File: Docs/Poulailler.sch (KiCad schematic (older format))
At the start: 13 parts, among them Q1 Q_PNP_ECB

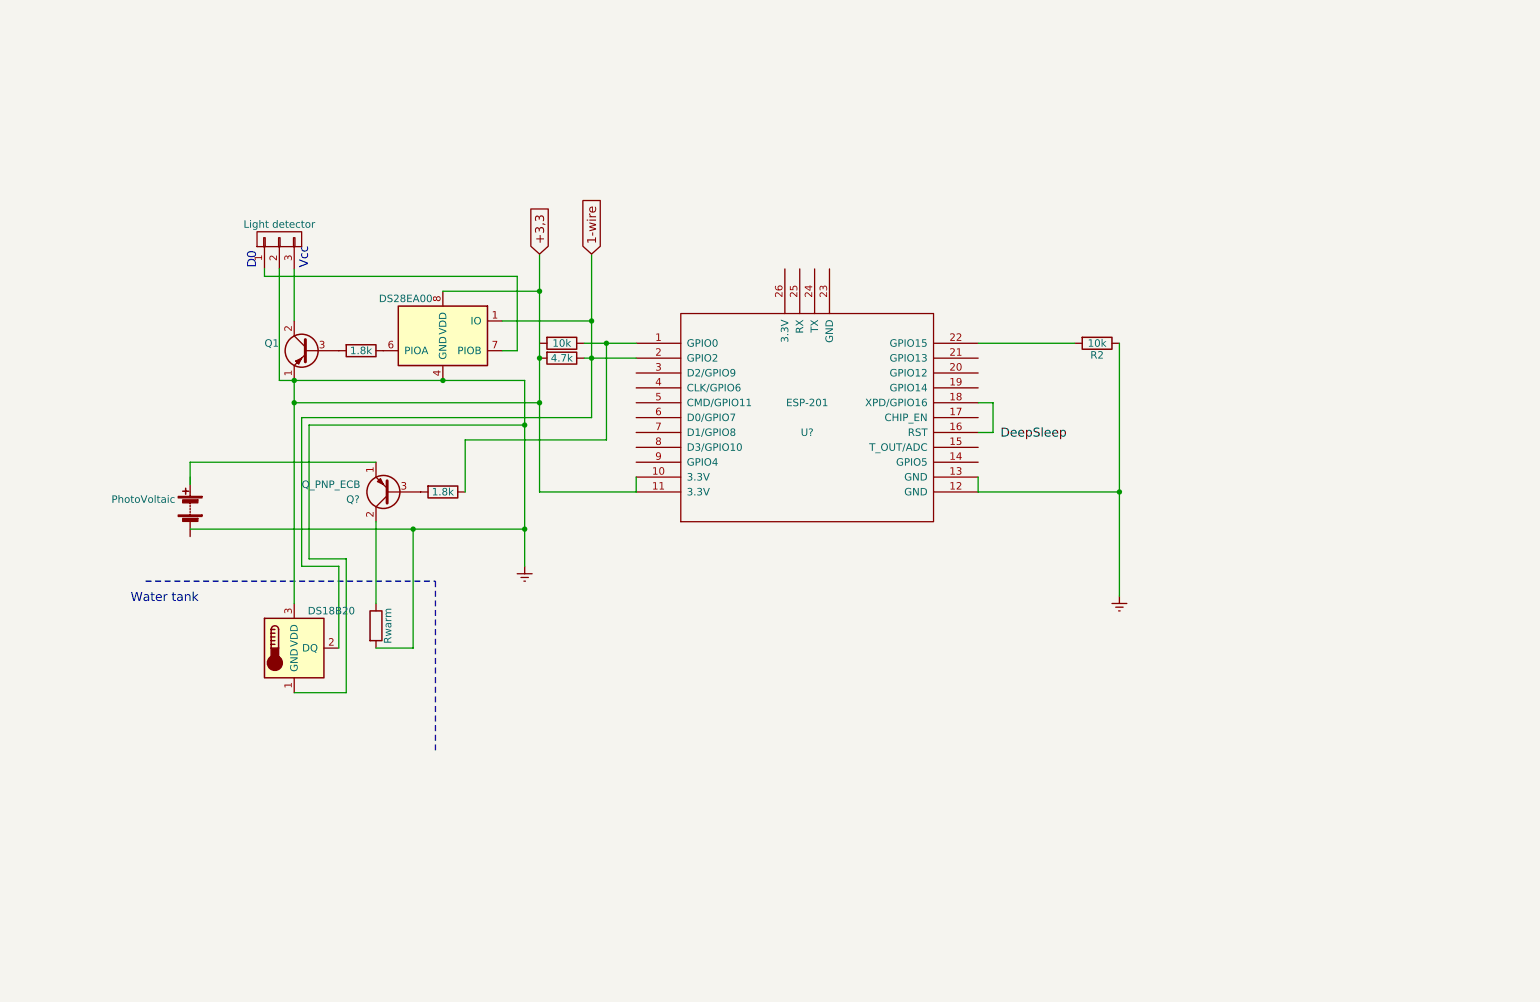
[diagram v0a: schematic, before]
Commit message: Split by function
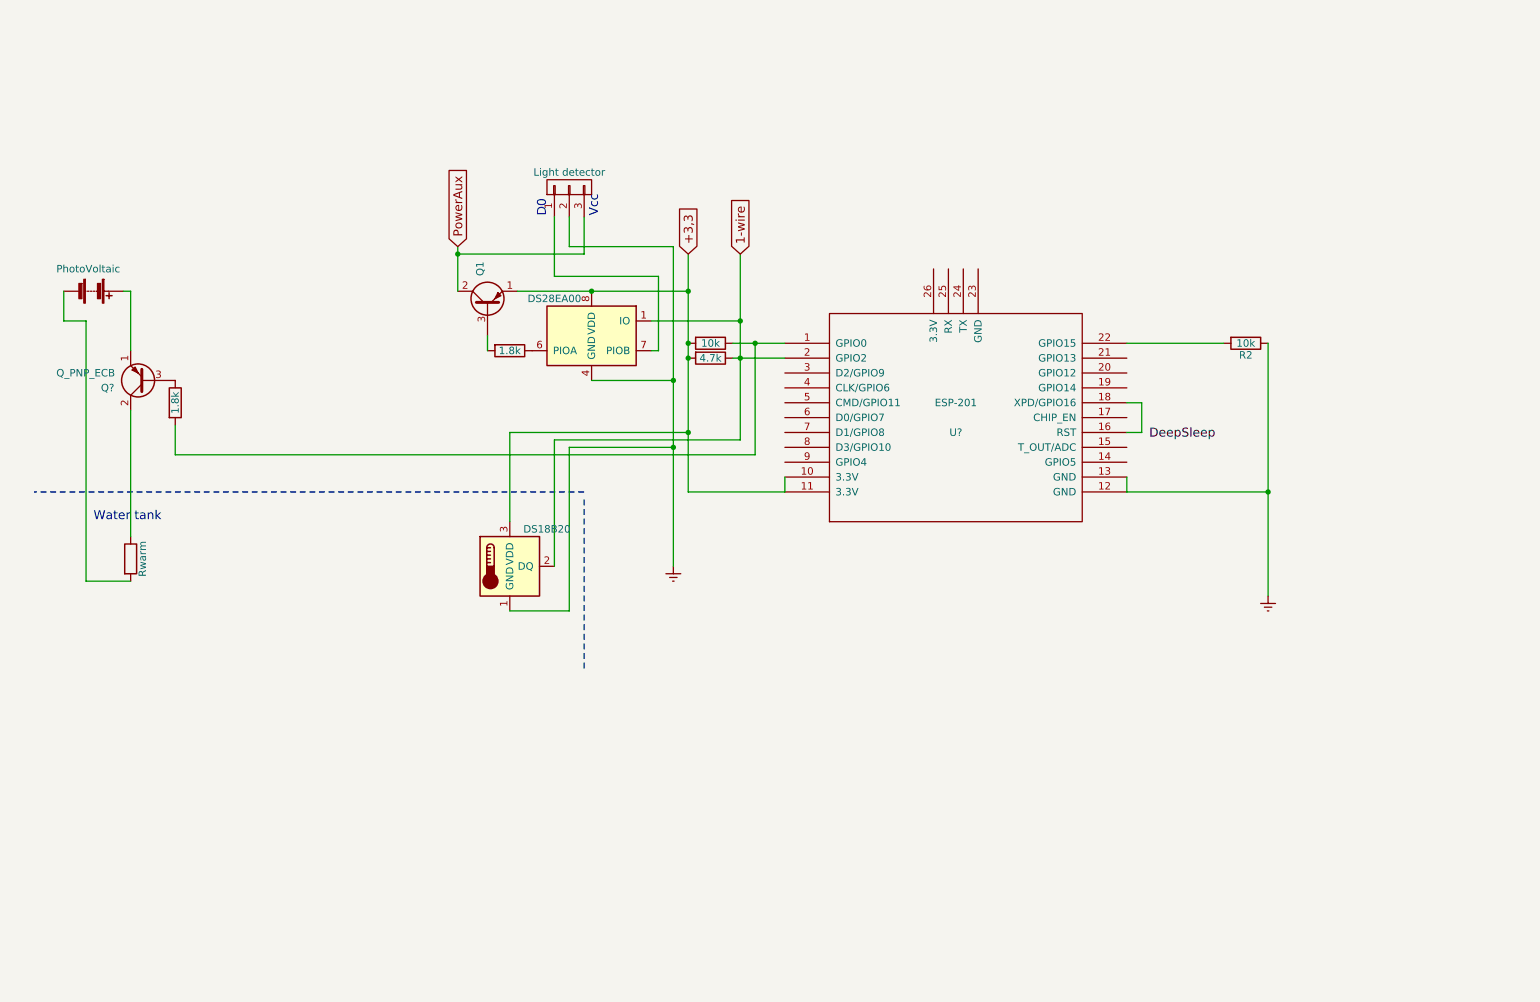
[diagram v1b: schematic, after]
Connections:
- net labels added: PowerAux
- wire segments 43 -> 44
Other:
- moved on the sheet: PhotoVoltaic, Q1, Q?, R2, Rwarm, U?

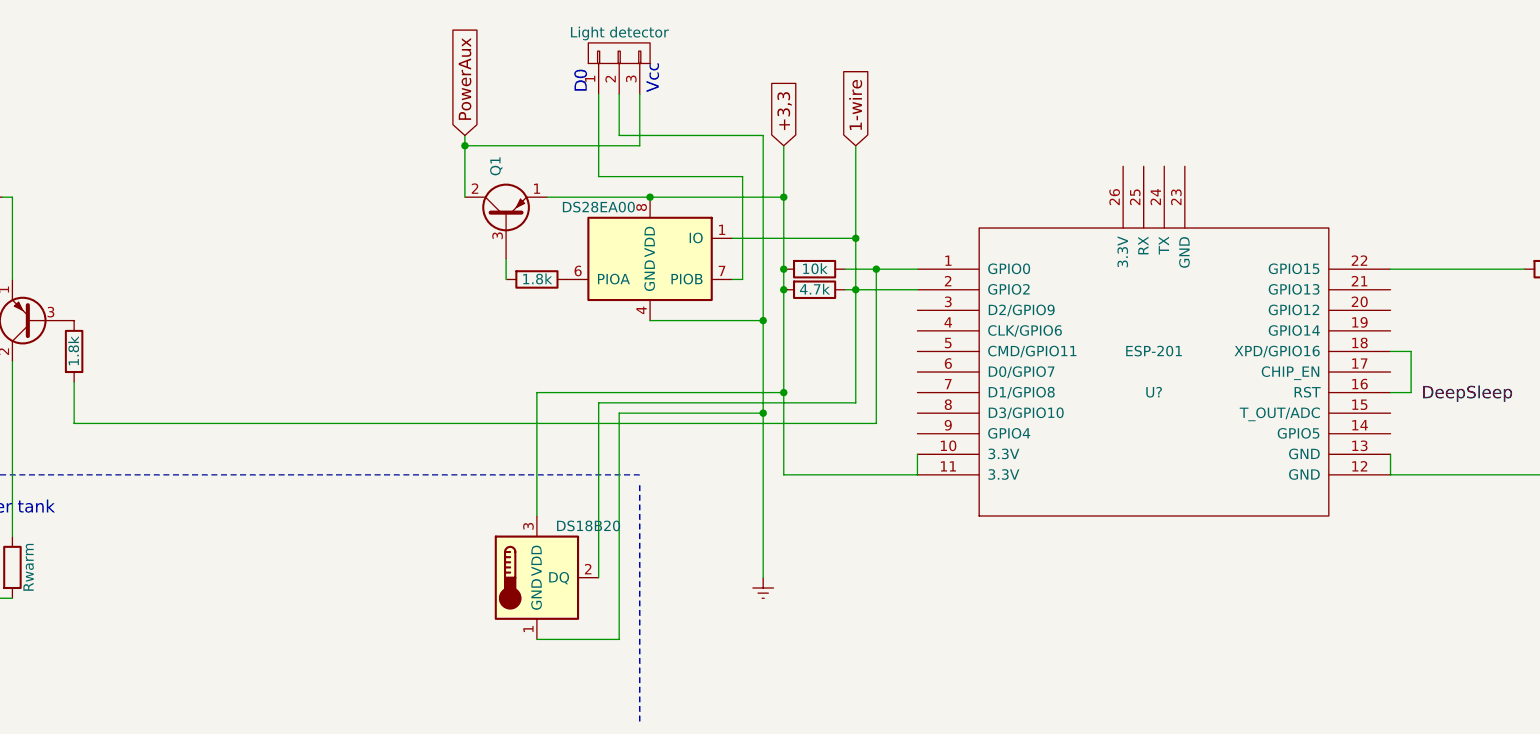
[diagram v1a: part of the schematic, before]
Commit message: Add water level detection
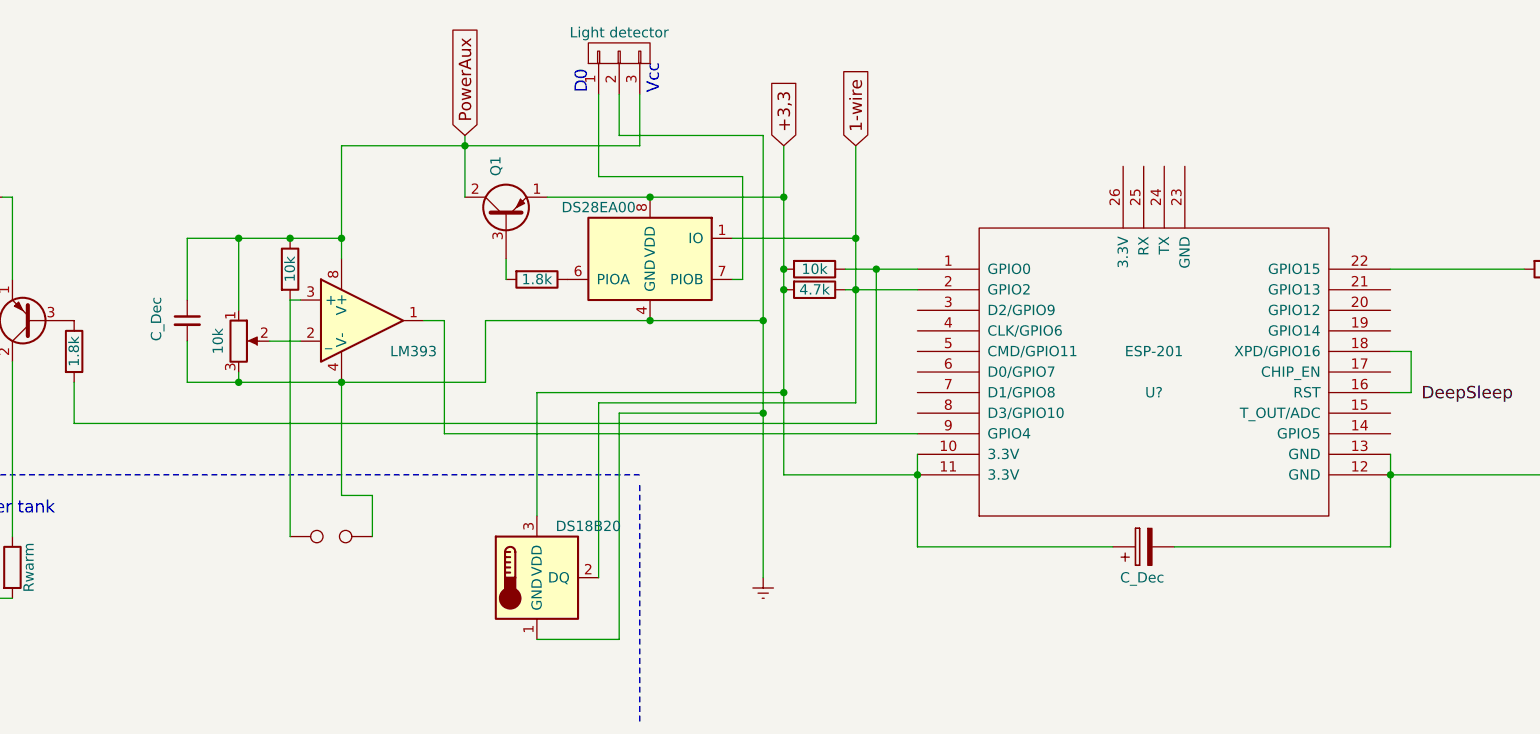
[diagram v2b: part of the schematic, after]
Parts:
- added C?: C_Dec, symbol C_Small
- added C?: C_Dec, symbol CP
- added R?: 10k, symbol R
- added RV?: 10k, symbol POT
- added U?: LM393, symbol LM393
- added W?: TEST, symbol TEST
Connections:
- net +3,3: now also C?.1
- net Earth: now also C?.2, C?.2, RV?.3, U?.4 (V-), W?.2
- net PowerAux: now also C?.1, R?.1, RV?.1, U?.8 (V+)
- net at U?.9 (GPIO4): now also U?.1
- new net: RV?.2, U?.2 (_)
- new net: R?.2, U?.3 (+), W?.1
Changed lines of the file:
@@
 	5200 3750 5850 3750
 Wire Wire Line
-	5850 3750 5850 3650
+	5850 3650 5850 4100
 Wire Wire Line
 	5500 2850 5850 2850
@@
 Connection ~ 5550 2850
 Wire Wire Line
-	8150 3650 8150 3750
+	8150 3650 8150 4100
 Wire Wire Line
 	8150 3750 9100 3750
@@
 	4400 2100 4400 1900
 Wire Wire Line
-	3650 2150 4500 2150
+	3050 2150 4500 2150
 Wire Wire Line
 	4500 2150 4500 1900
 Connection ~ 3650 2150
 Wire Wire Line
-	4550 3000 5100 3000
+	3750 3000 5100 3000
 Connection ~ 5100 3000
 Wire Wire Line
@@
 Wire Notes Line
 	4500 3750 800  3750
+$Comp
+L LM393 U?
+U 1 1 5A243E7D
+P 3150 3000
+F 0 "U?" H 3300 3150 50  0001 C CNN
+F 1 "LM393" H 3400 2850 50  0000 C CNN
+F 2 "" H 3150 3000 50  0000 C CNN
+F 3 "" H 3150 3000 50  0000 C CNN
+	1    3150 3000
+	1    0    0    -1
+$EndComp
+$Comp
+L POT RV?
+U 1 1 5A243FD7
+P 2550 3100
+F 0 "RV?" V 2375 3100 50  0001 C CNN
+F 1 "10k" V 2450 3100 50  0000 C CNN
+F 2 "" H 2550 3100 50  0001 C CNN
+F 3 "" H 2550 3100 50  0001 C CNN
+	1    2550 3100
+	1    0    0    -1
+$EndComp
+$Comp
+L R R?
+U 1 1 5A24433B
+P 2800 2750
+F 0 "R?" V 2880 2750 50  0001 C CNN
+F 1 "10k" V 2800 2750 50  0000 C CNN
+F 2 "" V 2730 2750 50  0001 C CNN
+F 3 "" H 2800 2750 50  0001 C CNN
+	1    2800 2750
+	1    0    0    -1
+$EndComp
+Wire Wire Line
+	3050 2700 3050 2150
+Wire Wire Line
+	2300 2600 3050 2600
+Connection ~ 3050 2600
+Wire Wire Line
+	2550 2600 2550 2950
+Wire Wire Line
+	2700 3100 2850 3100
+Wire Wire Line
+	2550 3250 2550 3300
+Wire Wire Line
+	2300 3300 3750 3300
+Wire Wire Line
+	3750 3300 3750 3000
+Connection ~ 4550 3000
+Connection ~ 3050 3300
+Wire Wire Line
+	3450 3000 3550 3000
+Wire Wire Line
+	3550 3000 3550 3550
+Wire Wire Line
+	3550 3550 5850 3550
+$Comp
+L TEST W?
+U 1 1 5A2445F7
+P 3000 4050
+F 0 "W?" H 3000 4110 50  0001 C CNN
+F 1 "TEST" H 3000 3980 50  0001 C CNN
+F 2 "" H 3000 4050 50  0000 C CNN
+F 3 "" H 3000 4050 50  0000 C CNN
+	1    3000 4050
+	1    0    0    -1
+$EndComp
+Wire Wire Line
+	2850 2900 2800 2900
+Wire Wire Line
+	2800 2900 2800 4050
+Wire Wire Line
+	3050 3300 3050 3850
+Wire Wire Line
+	3050 3850 3200 3850
+Wire Wire Line
+	3200 3850 3200 4050
+$Comp
+L C_Small C?
+U 1 1 5A24478E
+P 2300 3000
+F 0 "C?" H 2310 3070 50  0001 L CNN
+F 1 "C_Dec" V 2150 2900 50  0000 L CNN
+F 2 "" H 2300 3000 50  0001 C CNN
+F 3 "" H 2300 3000 50  0001 C CNN
+	1    2300 3000
+	1    0    0    -1
+$EndComp
+Connection ~ 2550 2600
+Connection ~ 2550 3300
+Wire Wire Line
+	2300 2600 2300 2900
+Wire Wire Line
+	2300 3100 2300 3300
+Connection ~ 2800 2600
+$Comp
+L CP C?
+U 1 1 5A2450FE
+P 6950 4100
+F 0 "C?" H 6975 4200 50  0001 L CNN
+F 1 "C_Dec" V 6800 4000 50  0000 L CNN
+F 2 "" H 6988 3950 50  0001 C CNN
+F 3 "" H 6950 4100 50  0001 C CNN
+	1    6950 4100
+	0    -1   -1   0
+$EndComp
+Wire Wire Line
+	5850 4100 6800 4100
+Connection ~ 5850 3750
+Wire Wire Line
+	8150 4100 7100 4100
+Connection ~ 8150 3750
 $EndSCHEMATC

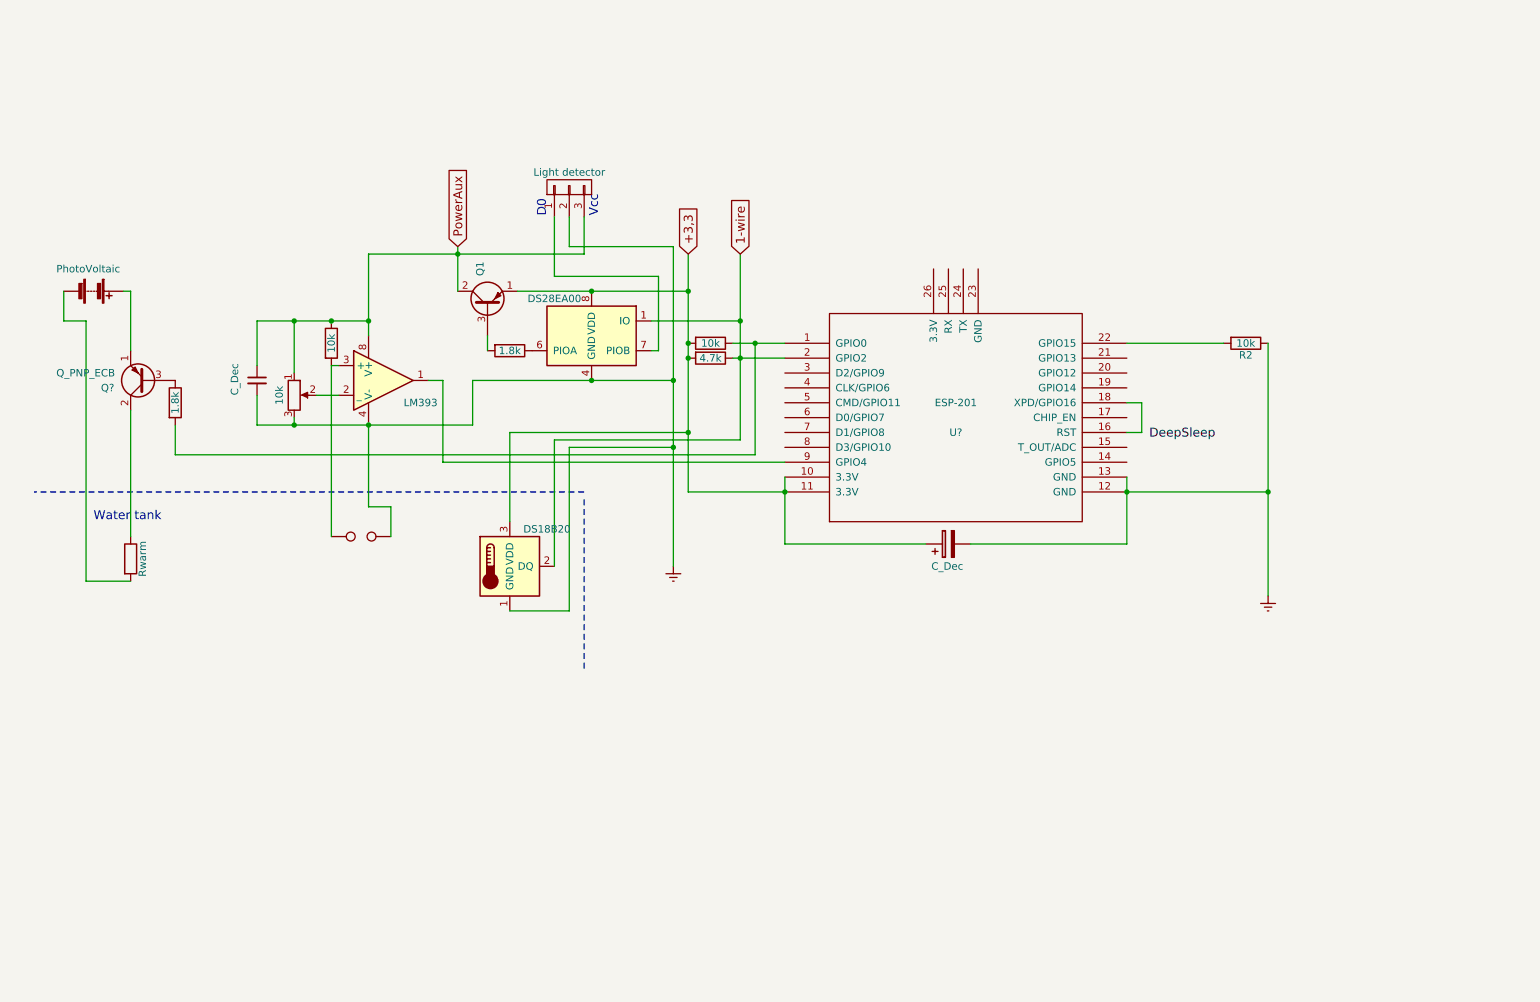
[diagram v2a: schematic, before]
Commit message: Schema completed
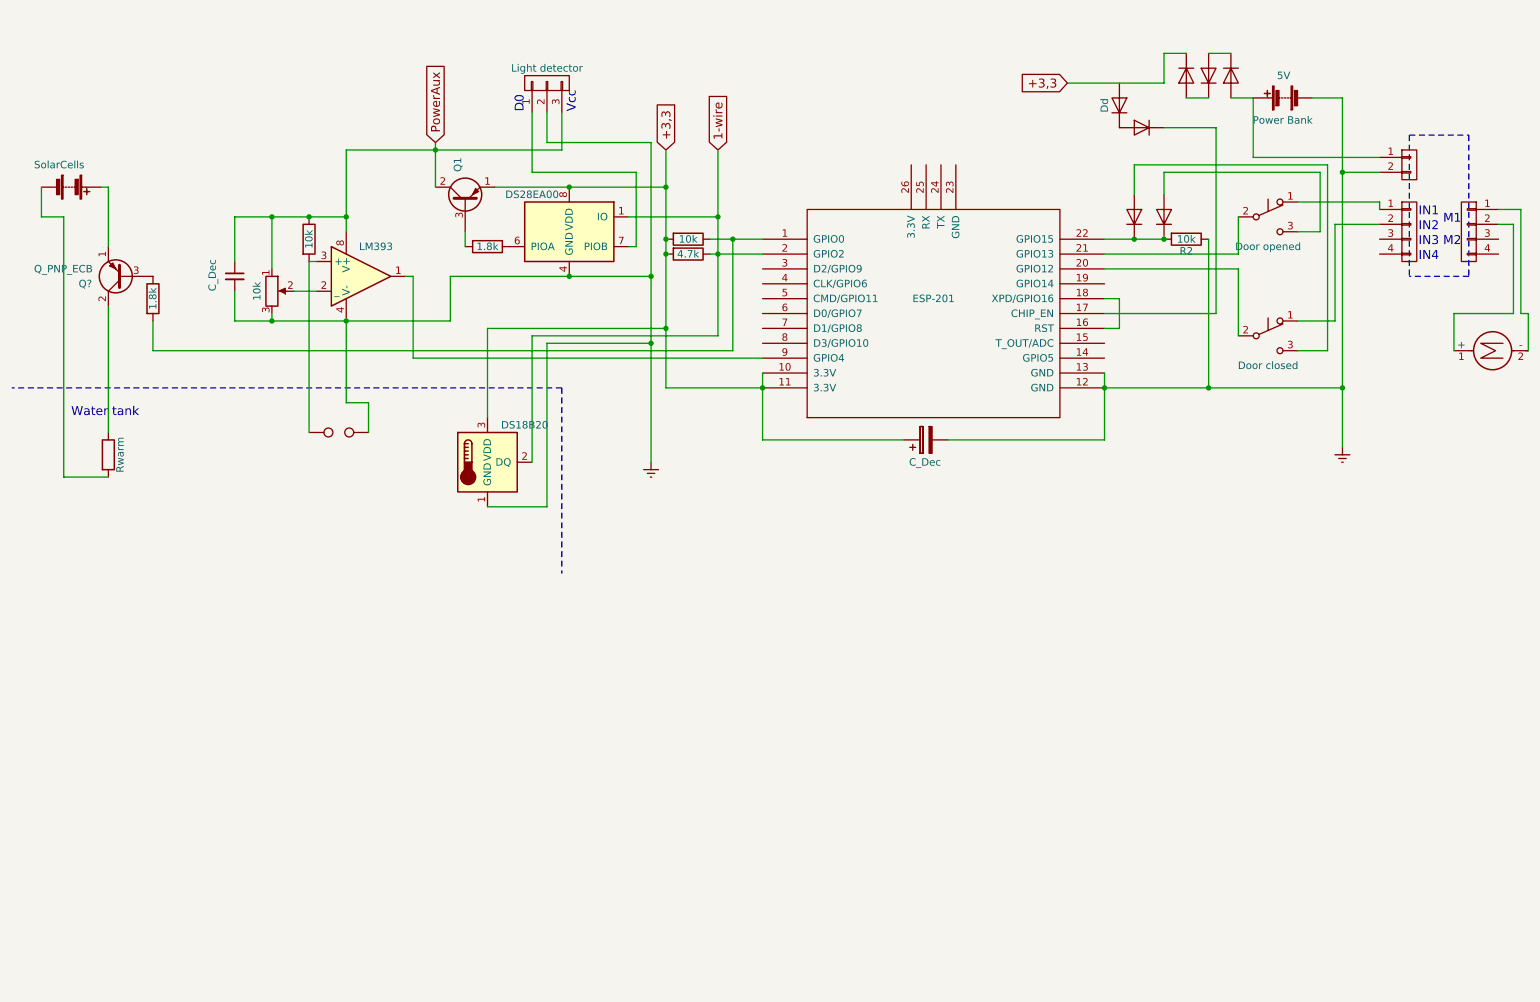
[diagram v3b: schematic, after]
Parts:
- added 5V: Power Bank, symbol Battery
- added D? (x6): D, symbol D
- added D?: Dd, symbol D
- added M?: Motor_DC, symbol Motor_DC
- added P? (x2): H bridge, symbol CONN_01X04
- added P?: CONN_01X02, symbol CONN_01X02
- added SW?: Door opened, symbol SW_Push_SPDT
- added SW?: Door closed, symbol SW_Push_SPDT
- renumbered PhotoVoltaic to SolarCells
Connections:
- net +3,3: now also D?.1 (K)
- net Earth: now also 5V.2 (-), P?.2 (P2)
- net at U?.17 (CHIP_EN): now also D?.1 (K)
- net at U?.20 (GPIO12): now also SW?.2 (B)
- net at U?.21 (GPIO13): now also SW?.2 (B)
- net at R2.2, U?.22 (GPIO15): now also D?.1 (K), D?.1 (K)
- new net: D?.2 (A), SW?.3 (C) (x2)
- new net: P?.1 (P1), SW?.1 (A)
- new net: P?.2 (P2), SW?.1 (A)
- new net: M?.2 (-), P?.1 (P1)
- new net: M?.1 (+), P?.2 (P2)
- new net: 5V.1 (+), D?.2 (A), P?.1 (P1)
- new net: D?.1 (K), D?.2 (A) (x3)
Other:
- note added: "IN1"
- note added: "IN2"
- note added: "IN3"
- note added: "IN4"
- note added: "M1"
- note added: "M2"
- moved on the sheet: Q1, Q?, R2, Rwarm, SolarCells
